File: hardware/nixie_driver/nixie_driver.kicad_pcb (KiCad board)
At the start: 2 copper layers, 46 parts, among them J2 Conn_02x05_Odd_Even, U1 CD40109B, U2 TubeClock_HV5622, U3 TubeClock_HV5622, U4 TubeClock_HV5622

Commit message: Inital PCB placement
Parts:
- removed H1, H2, H3, H4: MountingHole_Pad, MountingHole:MountingHole_3.2mm_M3_Pad_Via
- removed J2: Conn_02x05_Odd_Even, Connector_PinHeader_2.54mm:PinHeader_2x05_P2.54mm_Vertical
- added J1: Conn_01x03, Connector_PinHeader_2.54mm:PinHeader_1x03_P2.54mm_Vertical, F.Cu at (104.0, 53.9)
- added J3: Conn_01x03, Connector_PinHeader_2.54mm:PinHeader_1x03_P2.54mm_Vertical, F.Cu at (104.0, 85.5)
- added J4: Conn_02x03_Odd_Even, Connector_PinHeader_2.54mm:PinHeader_2x03_P2.54mm_Vertical, F.Cu at (261.5, 85.0)
- moved C3 214.4 mm to (252.0, 80.0), turned to 180 degrees
- moved R8 212.2 mm to (255.0, 54.8), turned to 90 degrees
- moved C1 210.7 mm to (246.0, 91.0), turned to -90 degrees
- moved R18 205.8 mm to (253.0, 56.8), turned to 90 degrees
- moved R25 205.4 mm to (257.0, 56.8), turned to 90 degrees
- moved U4 204.2 mm to (225.1, 86.0), turned to -90 degrees
- moved U1 203.4 mm to (252.0, 87.0)
- moved C5 197.2 mm to (234.0, 91.0), turned to -90 degrees
- moved R6 191.8 mm to (234.7, 54.8), turned to 90 degrees
- moved R17 185.4 mm to (232.7, 56.8), turned to 90 degrees
- moved R26 185.2 mm to (236.7, 56.8), turned to 90 degrees
- moved N8 177.2 mm to (255.0, 70.0), turned to 180 degrees
- moved N7 175.9 mm to (234.7, 70.0), turned to 180 degrees
- moved N6 174.6 mm to (214.4, 70.0), turned to 180 degrees
- moved N5 173.4 mm to (194.1, 70.0), turned to 180 degrees
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- renumbered N3 to N2, N5 to N3, N7 to N4, N2 to N5, N4 to N6, N6 to N7
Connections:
- R1 pad 2: VDD -> +HV
- R2 pad 2: VDD -> +HV
- R3 pad 2: VDD -> +HV
- R4 pad 2: VDD -> +HV
- R5 pad 2: VDD -> +HV
- R6 pad 2: VDD -> +HV
- R7 pad 2: VDD -> +HV
- R8 pad 2: VDD -> +HV
- U2 pad 23: /D_{OUT1} -> unconnected-(U2-DATA_OUT-Pad23)
- U2 pad 32: /D_{IN} -> /D_{OUT2}
- U4 pad 1: /NX8_RP -> /NX8_K0
- U4 pad 10: /NX7_K8 -> /NX7_K7
- U4 pad 11: /NX7_K9 -> /NX7_K8
- U4 pad 2: /NX7_LP -> /NX8_RP
- U4 pad 23: unconnected-(U4-DATA_OUT-Pad23) -> /D_{OUT1}
- U4 pad 3: /NX7_K1 -> /NX7_LP
- U4 pad 32: /D_{OUT2} -> /D_{IN}
- U4 pad 35: /NX8_K1 -> /NX8_LP
- U4 pad 36: /NX8_K2 -> /NX8_K1
- U4 pad 37: /NX8_K3 -> /NX8_K2
- U4 pad 38: /NX8_K4 -> /NX8_K3
- U4 pad 39: /NX8_K5 -> /NX8_K4
- U4 pad 4: /NX7_K2 -> /NX7_K1
- U4 pad 40: /NX8_K6 -> /NX8_K5
- U4 pad 41: /NX8_K7 -> /NX8_K6
- U4 pad 42: /NX8_K8 -> /NX8_K7
- U4 pad 43: /NX8_K9 -> /NX8_K8
- U4 pad 44: /NX8_K0 -> /NX8_K9
- U4 pad 5: /NX7_K3 -> /NX7_K2
- U4 pad 6: /NX7_K4 -> /NX7_K3
- U4 pad 7: /NX7_K5 -> /NX7_K4
- U4 pad 8: /NX7_K6 -> /NX7_K5
- U4 pad 9: /NX7_K7 -> /NX7_K6
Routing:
- net +HV: track 0.00 -> 151.0 mm
- net Net-(N3-PadA): track 0.00 -> 8.09 mm
- net Net-(N2-PadA): track 0.00 -> 8.09 mm
- net Net-(N5-PadA): track 0.00 -> 8.09 mm
- net Net-(N7-PadA): track 0.00 -> 8.09 mm
- net Net-(N4-PadA): track 0.00 -> 8.08 mm
- net Net-(N6-PadA): track 0.00 -> 8.08 mm
- net Net-(N8-PadA): track 0.00 -> 8.08 mm
- net Net-(N1-PadA): track 0.00 -> 8.08 mm
- net Net-(N5-PadRHDP): track 0.00 -> 7.23 mm
- net Net-(N3-PadRHDP): track 0.00 -> 7.21 mm
- net Net-(N2-PadLHDP): track 0.00 -> 7.21 mm
- net Net-(N7-PadRHDP): track 0.00 -> 7.21 mm
- net Net-(N4-PadRHDP): track 0.00 -> 7.20 mm
- net Net-(N6-PadLHDP): track 0.00 -> 7.20 mm
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
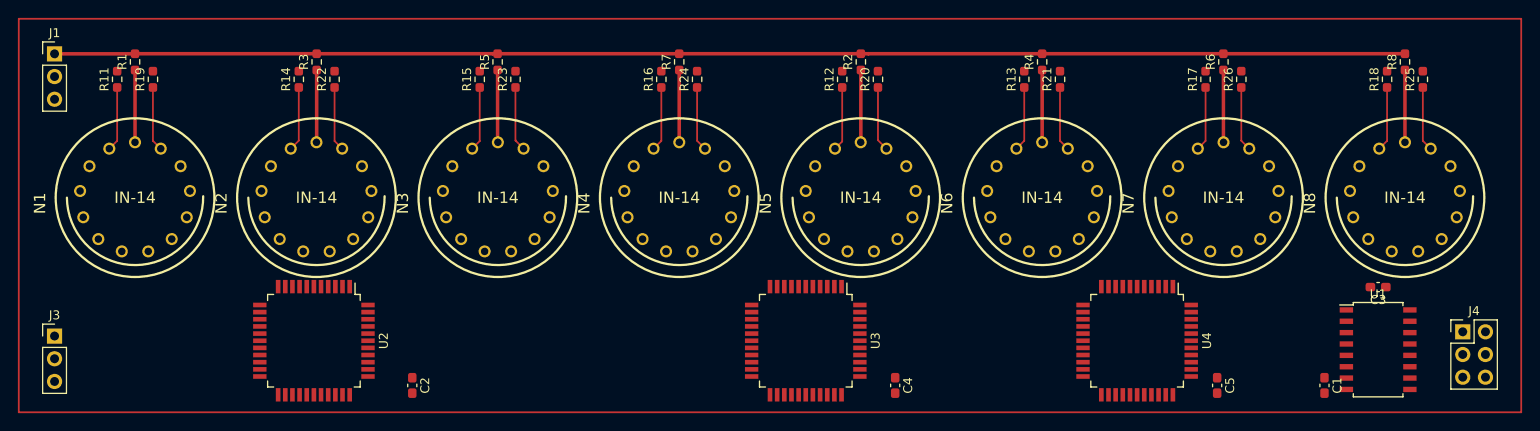
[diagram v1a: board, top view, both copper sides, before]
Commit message: PCB layout, traces for nixie_driver, 3 Nixies + logic
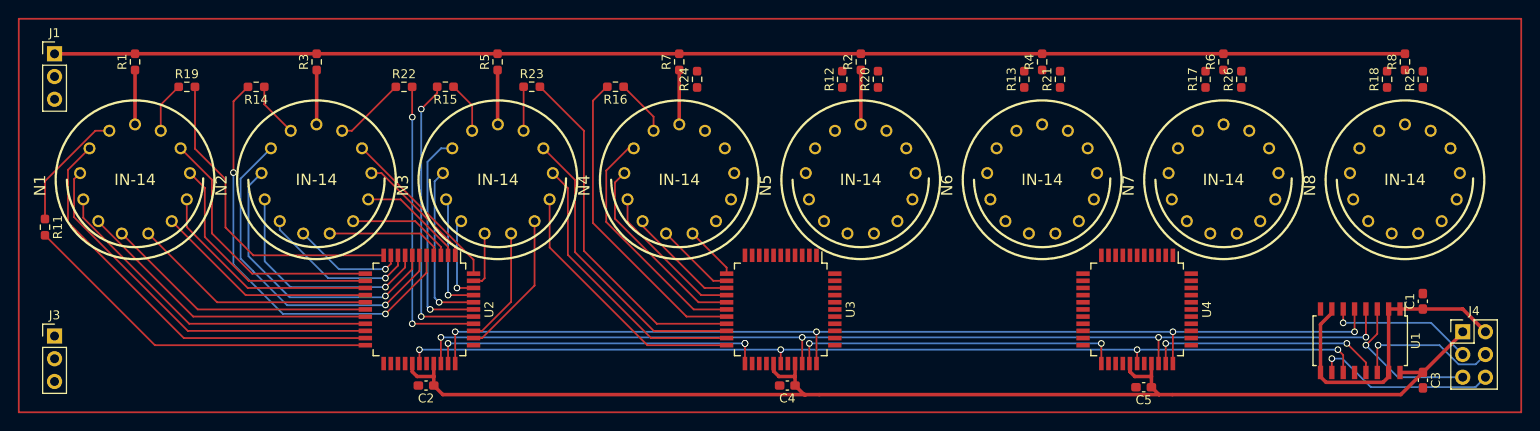
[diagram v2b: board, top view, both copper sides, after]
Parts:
- moved R11 18.4 mm to (102.9, 73.3), turned to -90 degrees
- moved C1 14.5 mm to (257.0, 81.6), turned to 90 degrees
- moved U2 12.3 mm to (144.8, 82.5)
- moved C4 12.1 mm to (185.9, 91.0), turned to 180 degrees
- moved C3 11.6 mm to (257.0, 90.4), turned to -90 degrees
- moved C5 8.21 mm to (225.8, 91.2), turned to 180 degrees
- moved R22 7.81 mm to (143.1, 57.6), turned to 0 degrees
- moved R16 5.20 mm to (166.7, 57.6), turned to 180 degrees
- moved R14 4.84 mm to (126.5, 57.6), turned to 180 degrees
- moved U3 4.48 mm to (185.2, 82.5)
- moved R15 3.93 mm to (147.7, 57.6), turned to 180 degrees
- moved R19 3.88 mm to (118.8, 57.6), turned to 0 degrees
- moved U4 3.50 mm to (225.1, 82.5)
- moved U1 2.24 mm to (250.0, 86.0), turned to -90 degrees
- moved R23 2.00 mm to (157.4, 57.6), turned to 0 degrees
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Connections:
- J4 pad 2: +3V3 -> +3.3V
- U2 pad 1: /NX2_K2 -> /NX2_K9
- U2 pad 10: /NX2_RP -> /NX2_K5
- U2 pad 11: /NX1_LP -> /NX1_RP
- U2 pad 12: /NX1_K1 -> /NX1_K0
- U2 pad 13: /NX1_K2 -> /NX1_K9
- U2 pad 14: /NX1_K3 -> /NX1_K8
- U2 pad 15: /NX1_K4 -> /NX1_K7
- U2 pad 16: /NX1_K5 -> /NX1_K6
- U2 pad 17: /NX1_K6 -> /NX1_K5
- U2 pad 18: /NX1_K7 -> /NX1_K4
- U2 pad 19: /NX1_K8 -> /NX1_K3
- U2 pad 2: /NX2_K3 -> /NX2_K8
- U2 pad 20: /NX1_K9 -> /NX1_K2
- U2 pad 21: /NX1_K0 -> /NX1_K1
- U2 pad 22: /NX1_RP -> /NX1_LP
- U2 pad 3: /NX2_K4 -> /NX2_K7
- U2 pad 35: /NX3_K4 -> /NX3_K7
- U2 pad 36: /NX3_K5 -> /NX3_K6
- U2 pad 37: /NX3_K6 -> /NX2_RP
- U2 pad 38: /NX3_K7 -> /NX3_LP
- U2 pad 39: /NX3_K8 -> /NX3_K1
- U2 pad 4: /NX2_K5 -> /NX2_K6
- U2 pad 40: /NX3_K9 -> /NX3_K2
- U2 pad 41: /NX3_K0 -> /NX3_K3
- U2 pad 42: /NX3_RP -> /NX3_K4
- U2 pad 43: /NX2_LP -> /NX3_K5
- U2 pad 44: /NX2_K1 -> /NX2_K0
- U2 pad 5: /NX2_K6 -> /NX2_LP
- U2 pad 6: /NX2_K7 -> /NX2_K1
- U2 pad 7: /NX2_K8 -> /NX2_K2
- U2 pad 8: /NX2_K9 -> /NX2_K3
- U2 pad 9: /NX2_K0 -> /NX2_K4
- U3 pad 12: /NX4_K5 -> /NX4_K6
- U3 pad 13: /NX4_K6 -> /NX4_K5
- U3 pad 14: /NX4_K7 -> /NX4_K4
- U3 pad 15: /NX4_K8 -> /NX4_K3
- U3 pad 16: /NX4_K9 -> /NX4_K2
- U3 pad 17: /NX4_K0 -> /NX4_K1
- U3 pad 18: /NX4_RP -> /NX4_LP
- U3 pad 19: /NX3_LP -> /NX3_RP
- U3 pad 20: /NX3_K1 -> /NX3_K0
- U3 pad 21: /NX3_K2 -> /NX3_K9
- U3 pad 22: /NX3_K3 -> /NX3_K8
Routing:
- net +12V: track 0.00 -> 142.0 mm
- net /~{LE}: track 0.00 -> 115.4 mm, vias 0 -> 4
- net /~{BL}: track 0.00 -> 113.8 mm, vias 0 -> 4
- net /CLK: track 0.00 -> 110.1 mm, vias 0 -> 4
- net /NX2_LP: track 0.00 -> 48.4 mm, vias 0 -> 2
- net /NX1_K1: track 0.00 -> 47.9 mm
- net /NX1_K2: track 0.00 -> 43.0 mm
- net /NX1_LP: track 0.00 -> 40.9 mm
- net /NX3_RP: track 0.00 -> 39.7 mm
- net /NX2_K1: track 0.00 -> 39.3 mm, vias 0 -> 1
- net /NX1_K3: track 0.00 -> 38.5 mm
- net /D_{OUT2}: track 0.00 -> 37.7 mm, vias 0 -> 3
- net /D_{OUT1}: track 0.00 -> 37.2 mm, vias 0 -> 2
- net /NX1_RP: track 0.00 -> 36.1 mm
- net +3.3V: track 0.00 -> 35.7 mm
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
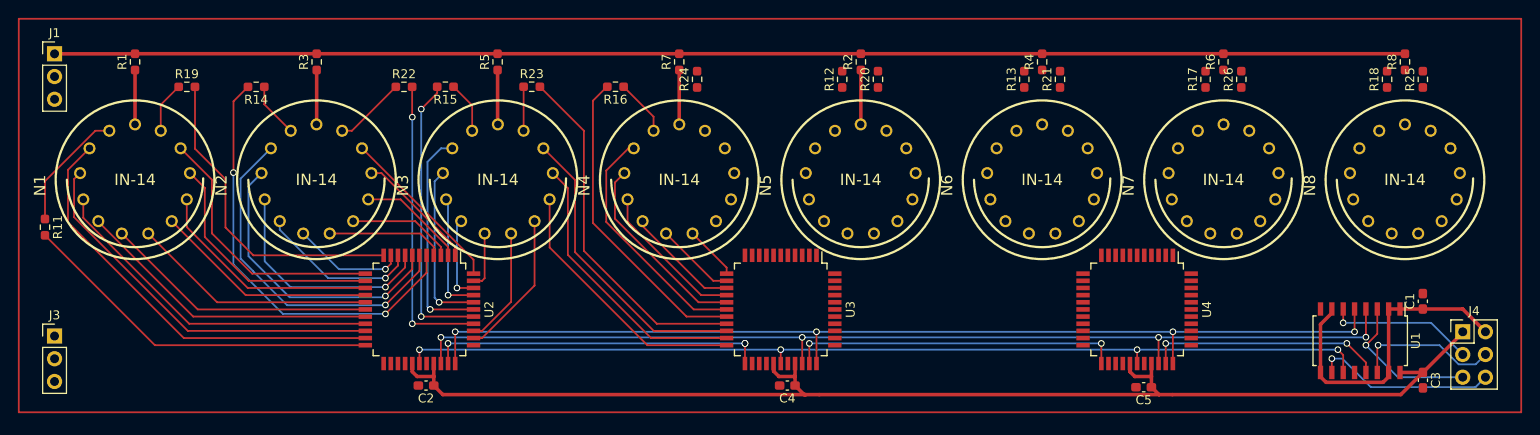
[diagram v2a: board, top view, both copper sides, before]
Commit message: Finish PCB design for nixie_driver
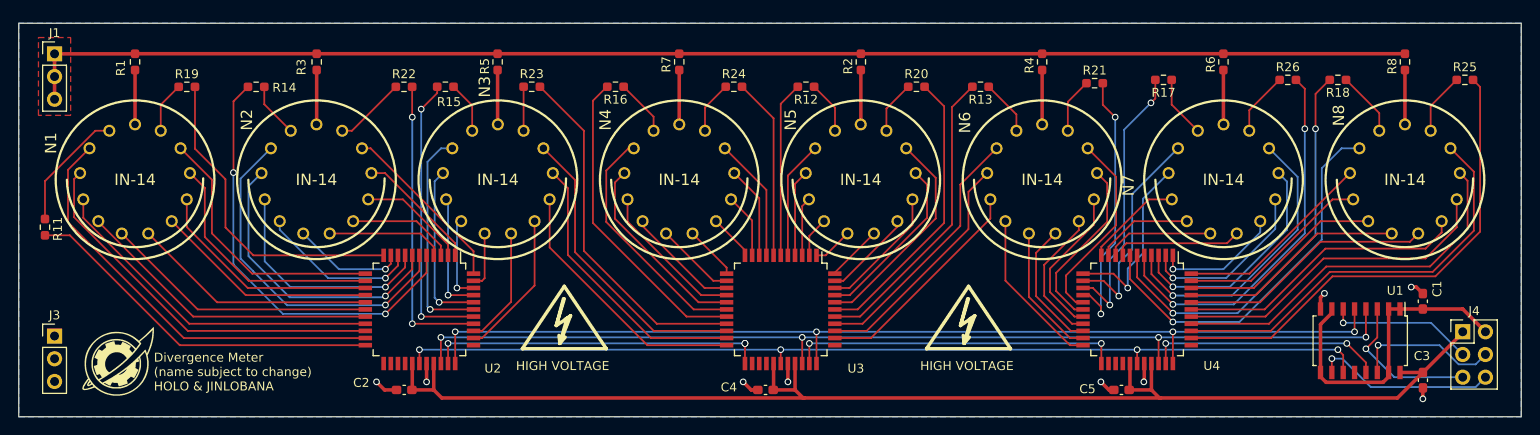
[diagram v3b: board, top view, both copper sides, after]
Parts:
- added IMG1: LOGO, GRAPHICS:future_gadget_lab_neg_tiny, F.Cu at (111.1, 88.3)
- added REF**: Symbol_HighVoltage_Type2_SilkTop_VerySmall, GRAPHICS:Symbol_HighVoltage_Type2_SilkTop_VerySmall, F.Cu at (206.2, 84.1)
- added REF**: Symbol_HighVoltage_Type2_SilkTop_VerySmall, GRAPHICS:Symbol_HighVoltage_Type2_SilkTop_VerySmall, F.Cu at (161.0, 84.1)
- moved R18 5.50 mm to (247.5, 56.8), turned to 180 degrees
- moved R26 5.20 mm to (241.9, 56.8), turned to 0 degrees
- moved R13 4.96 mm to (207.5, 57.6), turned to 180 degrees
- moved R17 4.70 mm to (228.0, 56.8), turned to 180 degrees
- moved R25 4.70 mm to (261.7, 56.8), turned to 0 degrees
- moved R20 4.38 mm to (200.4, 57.6), turned to 0 degrees
- moved R24 4.19 mm to (180.0, 57.6), turned to 0 degrees
- moved R12 4.14 mm to (188.0, 57.6), turned to 180 degrees
- moved R21 3.89 mm to (220.3, 57.2), turned to 0 degrees
- moved C5 2.51 mm to (223.3, 91.5)
- moved C2 2.49 mm to (143.1, 91.5)
- moved C4 2.49 mm to (183.5, 91.5)
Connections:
- U3 pad 1: /NX5_K6 -> /NX5_K5
- U3 pad 10: /NX4_K3 -> /NX4_K8
- U3 pad 11: /NX4_K4 -> /NX4_K7
- U3 pad 2: /NX5_K7 -> /NX5_K4
- U3 pad 3: /NX5_K8 -> /NX5_K3
- U3 pad 35: /NX6_K8 -> /NX6_K3
- U3 pad 36: /NX6_K9 -> /NX6_K2
- U3 pad 37: /NX6_K0 -> /NX6_K1
- U3 pad 38: /NX6_RP -> /NX6_LP
- U3 pad 39: /NX5_LP -> /NX5_RP
- U3 pad 4: /NX5_K9 -> /NX5_K2
- U3 pad 40: /NX5_K1 -> /NX5_K0
- U3 pad 41: /NX5_K2 -> /NX5_K9
- U3 pad 42: /NX5_K3 -> /NX5_K8
- U3 pad 43: /NX5_K4 -> /NX5_K7
- U3 pad 44: /NX5_K5 -> /NX5_K6
- U3 pad 5: /NX5_K0 -> /NX5_K1
- U3 pad 6: /NX5_RP -> /NX5_LP
- U3 pad 7: /NX4_LP -> /NX4_RP
- U3 pad 8: /NX4_K1 -> /NX4_K0
- U3 pad 9: /NX4_K2 -> /NX4_K9
- U4 pad 1: /NX8_K0 -> /NX7_K7
- U4 pad 10: /NX7_K7 -> /NX7_K4
- U4 pad 11: /NX7_K8 -> /NX7_K3
- U4 pad 12: /NX7_K9 -> /NX7_K2
- U4 pad 13: /NX7_K0 -> /NX7_K1
- U4 pad 14: /NX7_RP -> /NX7_LP
- U4 pad 15: /NX6_LP -> /NX6_RP
- U4 pad 16: /NX6_K1 -> /NX6_K0
- U4 pad 17: /NX6_K2 -> /NX6_K9
- U4 pad 18: /NX6_K3 -> /NX6_K8
- U4 pad 19: /NX6_K4 -> /NX6_K7
- U4 pad 2: /NX8_RP -> /NX7_K8
- U4 pad 20: /NX6_K5 -> /NX6_K6
- U4 pad 21: /NX6_K6 -> /NX6_K5
- U4 pad 22: /NX6_K7 -> /NX6_K4
- U4 pad 3: /NX7_LP -> /NX7_K9
- U4 pad 35: /NX8_LP -> /NX8_RP
- U4 pad 36: /NX8_K1 -> /NX8_K0
- U4 pad 37: /NX8_K2 -> /NX8_K9
- U4 pad 38: /NX8_K3 -> /NX8_K8
- U4 pad 39: /NX8_K4 -> /NX8_K7
- U4 pad 4: /NX7_K1 -> /NX7_K0
- U4 pad 40: /NX8_K5 -> /NX8_K6
- U4 pad 41: /NX8_K6 -> /NX8_K5
- U4 pad 42: /NX8_K7 -> /NX8_K4
- U4 pad 43: /NX8_K8 -> /NX8_K3
- U4 pad 44: /NX8_K9 -> /NX8_K2
- U4 pad 5: /NX7_K2 -> /NX7_RP
- U4 pad 6: /NX7_K3 -> /NX8_LP
- U4 pad 7: /NX7_K4 -> /NX8_K1
- U4 pad 8: /NX7_K5 -> /NX7_K6
- U4 pad 9: /NX7_K6 -> /NX7_K5
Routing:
- net /NX8_RP: track 0.00 -> 54.5 mm
- net /NX8_K0: track 0.00 -> 46.5 mm
- net /NX8_LP: track 0.00 -> 45.3 mm, vias 0 -> 2
- net /NX8_K1: track 0.00 -> 43.0 mm, vias 0 -> 1
- net /NX7_RP: track 0.00 -> 42.4 mm, vias 0 -> 2
- net /NX8_K9: track 0.00 -> 41.9 mm
- net /NX8_K8: track 0.00 -> 36.9 mm
- net /NX6_LP: track 0.00 -> 33.7 mm
- net /NX7_K0: track 0.00 -> 32.9 mm, vias 0 -> 1
- net /NX8_K7: track 0.00 -> 32.8 mm
- net /NX5_RP: track 0.00 -> 32.4 mm
- net /NX7_LP: track 0.00 -> 31.1 mm, vias 0 -> 2
- net /NX6_RP: track 0.00 -> 30.5 mm, vias 0 -> 2
- net /NX6_K1: track 0.00 -> 28.9 mm
- net /NX8_K6: track 0.00 -> 28.6 mm
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- added copper zone on F.Cu, net +HV
- added copper zone on B.Cu, net GND
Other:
- board outline added: 168 x 44 mm
- board text added: "Divergence Meter (name subject to change) HOLO & JINLOBANA"
- board text added: "HIGH VOLTAGE"

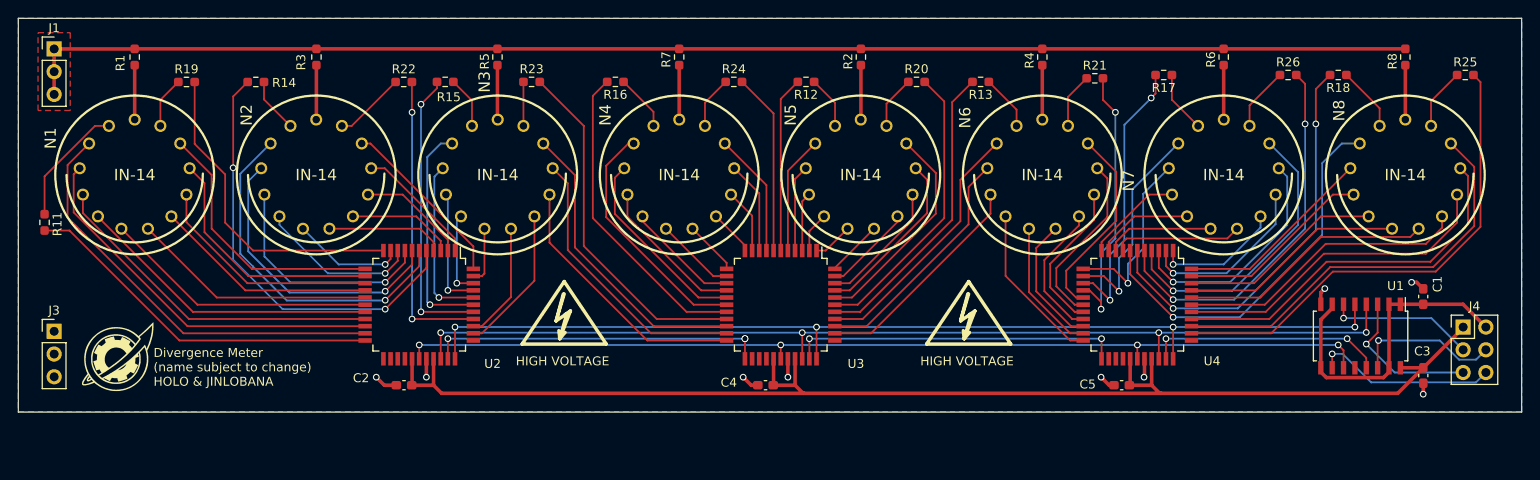
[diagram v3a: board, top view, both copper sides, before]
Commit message: Troubleshooting logic board design, begin component placement, fix positioning of board connectors
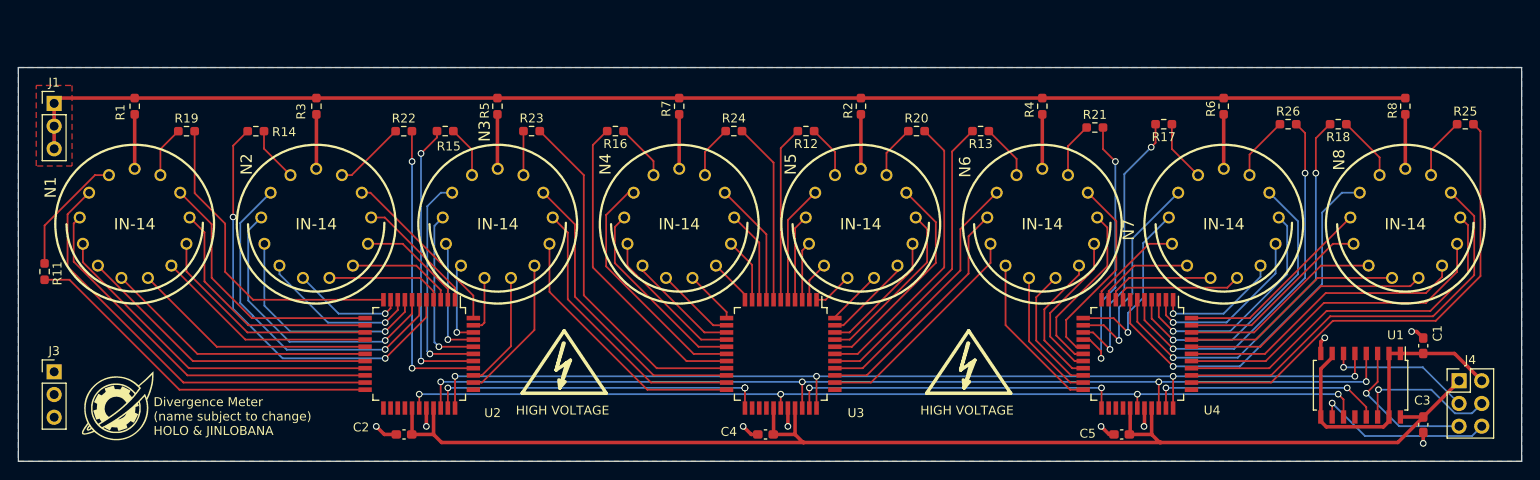
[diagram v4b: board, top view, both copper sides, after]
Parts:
- moved J1 6.08 mm to (104.0, 60.0)
- moved J4 6.02 mm to (261.0, 91.0)
- moved C1 5.50 mm to (257.0, 87.1)
- moved C2 5.50 mm to (143.1, 97.0)
- moved C3 5.50 mm to (257.0, 95.9)
- moved C4 5.50 mm to (183.5, 97.0)
- moved C5 5.50 mm to (223.3, 97.0)
- moved IMG1 5.50 mm to (111.1, 93.8)
- moved N1 5.50 mm to (113.0, 73.5)
- moved N2 5.50 mm to (133.3, 73.5)
- moved N3 5.50 mm to (153.6, 73.5)
- moved N4 5.50 mm to (173.9, 73.5)
- moved N5 5.50 mm to (194.1, 73.5)
- moved N6 5.50 mm to (214.4, 73.5)
- moved N7 5.50 mm to (234.7, 73.5)
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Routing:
- net +12V: track 149.0 -> 148.5 mm
